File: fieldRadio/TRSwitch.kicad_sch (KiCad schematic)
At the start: 36 parts, among them Q1 MMBT3904, Q2 MMBT3904, Q3 PMV240SP, Q5 MMBT3904, Q6 PMV240SP, Q7 BSS138

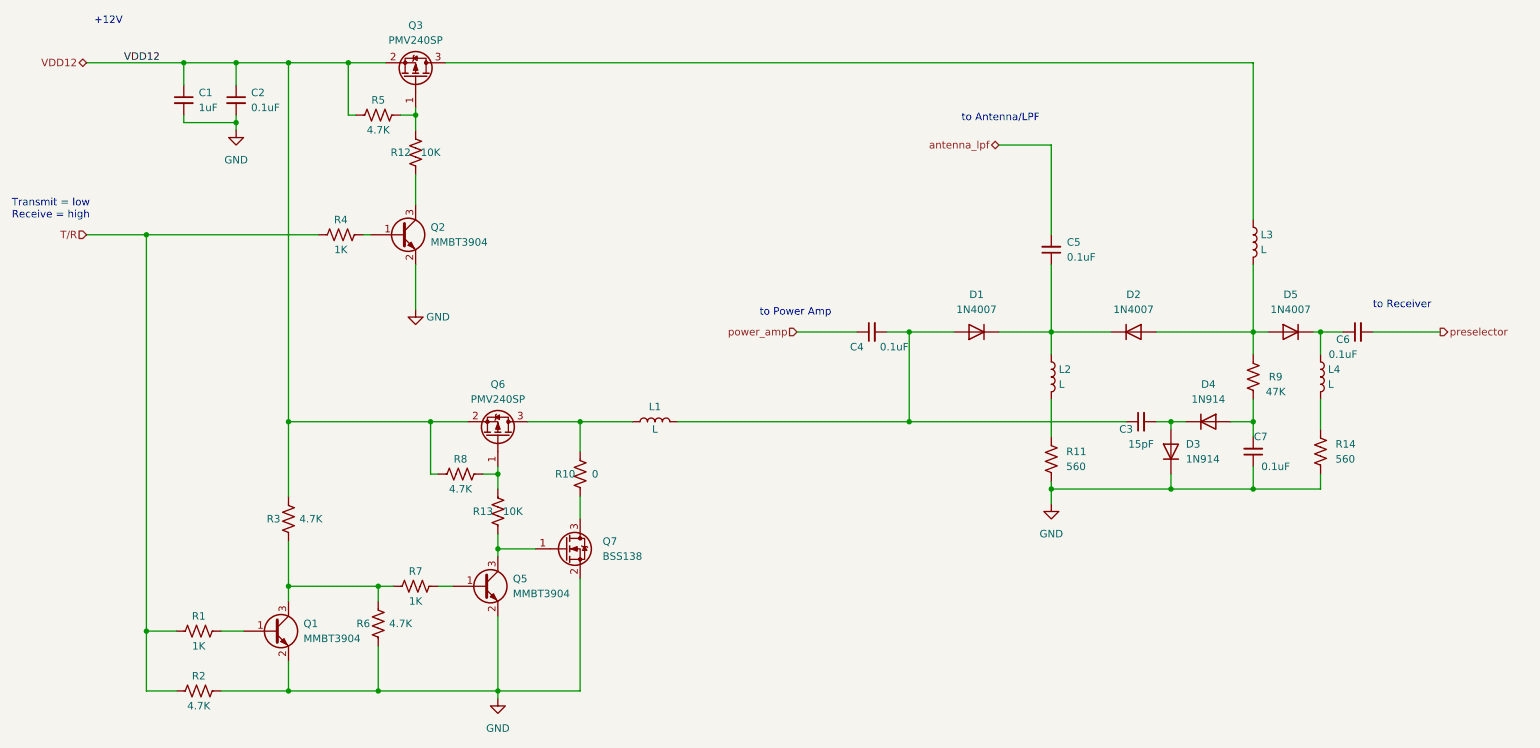
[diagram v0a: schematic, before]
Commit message: Building fieldradio schematic
in process of building field radio schematics
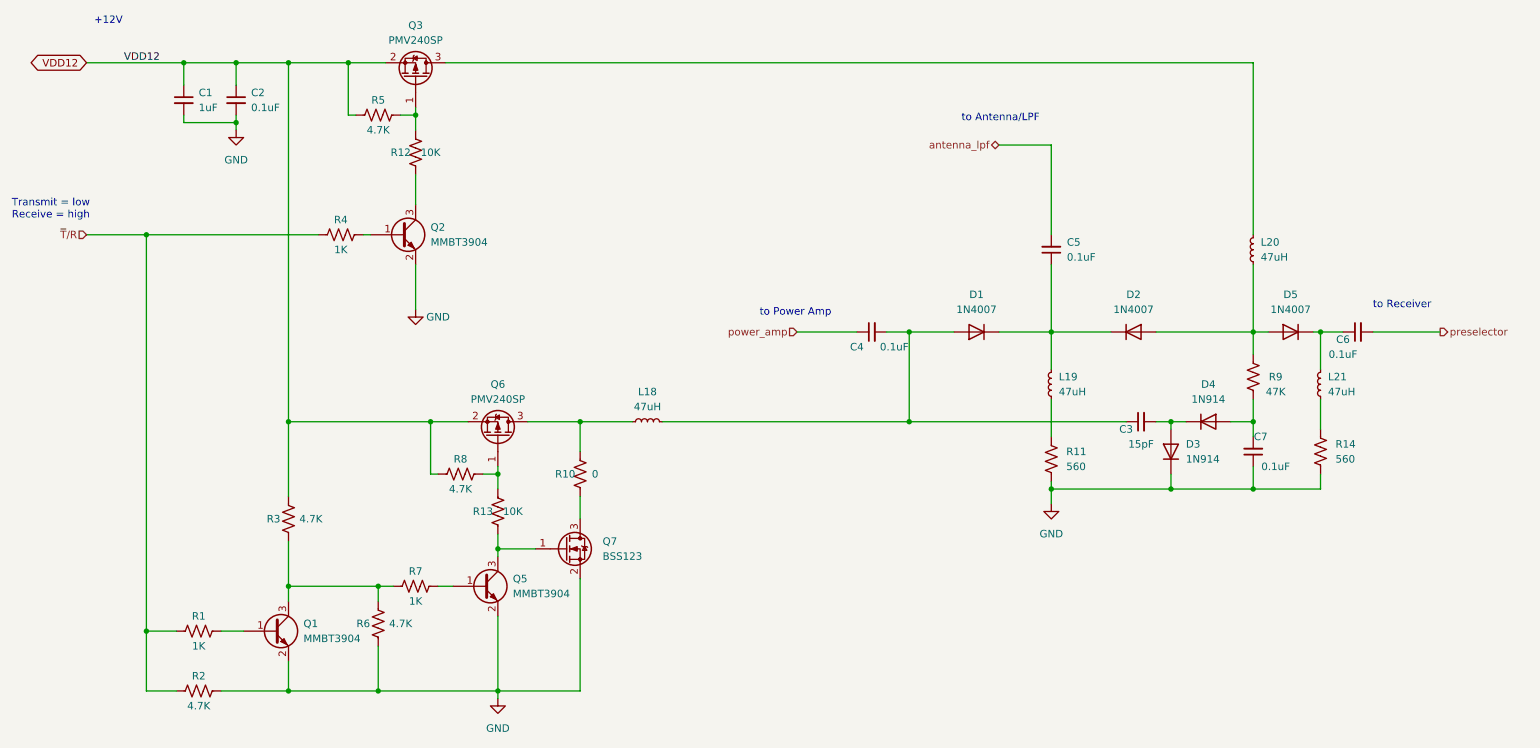
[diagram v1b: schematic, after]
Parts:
- removed L1, L2, L3, L4: L, Inductor_THT:L_Toroid_Vertical_L10.0mm_W5.0mm_P5.08mm, symbol Device:L
- added L18, L19, L20, L21: 47uH, Inductor_THT:L_Axial_L11.0mm_D4.5mm_P7.62mm_Vertical_Fastron_MECC, symbol Device:L_Small
- Q7: value BSS138 -> BSS123
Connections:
- net at C5.1, D1.1 (K), D2.1 (K): now also L19.2
- net at D2.2 (A), D5.2 (A), R9.2: now also L20.1
- net at R11.1: now also L19.1
- net at C3.1, C4.2, D1.2 (A): now also L18.2
- net at Q3.3 (D): now also L20.2
- net at Q6.3 (D), R10.2: now also L18.1
- net at R14.1: now also L21.1
- net at C6.1, D5.1 (K): now also L21.2
- net T/R renamed ~{T}/R

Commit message: More schematic dev.
More schematic development
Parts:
- renumbered L18 to L1, L19 to L2, L20 to L3, L21 to L4
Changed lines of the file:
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@@
       (project "fieldRadio"
         (path "/a1d1b2b0-2f27-4dc0-94ba-bb0e02933617/07223125-3b0c-43ef-b5d7-ce26f2ddaddd"
-          (reference "Q5") (unit 1)
+          (reference "Q4") (unit 1)
         )
       )
@@
       (project "fieldRadio"
         (path "/a1d1b2b0-2f27-4dc0-94ba-bb0e02933617/07223125-3b0c-43ef-b5d7-ce26f2ddaddd"
-          (reference "Q7") (unit 1)
+          (reference "Q6") (unit 1)
         )
       )
@@
       (project "fieldRadio"
         (path "/a1d1b2b0-2f27-4dc0-94ba-bb0e02933617/07223125-3b0c-43ef-b5d7-ce26f2ddaddd"
-          (reference "R11") (unit 1)
+          (reference "R12") (unit 1)
         )
       )
@@
       (project "fieldRadio"
         (path "/a1d1b2b0-2f27-4dc0-94ba-bb0e02933617/07223125-3b0c-43ef-b5d7-ce26f2ddaddd"
+          (reference "C3") (unit 1)
+        )
+      )
+    )
+  )
+  (symbol (lib_id "Device:C_Small") (at 265.43 100.33 180) (unit 1)
+    (in_bom yes) (on_board yes) (dnp no)
+    (property "Reference" "C5" (at 269.24 99.06 0)
+      (effects (font (size 1.27 1.27)))
+    )
+    (property "Value" "0.1uF" (at 270.51 101.6 0)
+      (effects (font (size 1.27 1.27)))
+    )
+    (property "Footprint" "Capacitor_THT:C_Disc_D5.0mm_W2.5mm_P5.00mm" (at 265.43 100.33 0)
+      (effects (font (size 1.27 1.27)) hide)
+    )
+    (property "Datasheet" "~" (at 265.43 100.33 0)
+      (effects (font (size 1.27 1.27)) hide)
+    )
+    (pin "1")
+    (pin "2")
+    (instances
+      (project ""
+        (path "/6f2c3d19-d4e9-42f1-a4a4-8f8c301ff52b"
+          (reference "C5") (unit 1)
+        )
+      )
+      (project "fieldRadio"
+        (path "/a1d1b2b0-2f27-4dc0-94ba-bb0e02933617/07223125-3b0c-43ef-b5d7-ce26f2ddaddd"
           (reference "C4") (unit 1)
         )
@@
     )
   )
-  (symbol (lib_id "Device:C_Small") (at 265.43 100.33 180) (unit 1)
-    (in_bom yes) (on_board yes) (dnp no)
-    (property "Reference" "C5" (at 269.24 99.06 0)
-      (effects (font (size 1.27 1.27)))
-    )
-    (property "Value" "0.1uF" (at 270.51 101.6 0)
-      (effects (font (size 1.27 1.27)))
-    )
-    (property "Footprint" "Capacitor_THT:C_Disc_D5.0mm_W2.5mm_P5.00mm" (at 265.43 100.33 0)
-      (effects (font (size 1.27 1.27)) hide)
-    )
-    (property "Datasheet" "~" (at 265.43 100.33 0)
-      (effects (font (size 1.27 1.27)) hide)
-    )
-    (pin "1")
-    (pin "2")
-    (instances
-      (project ""
-        (path "/6f2c3d19-d4e9-42f1-a4a4-8f8c301ff52b"
-          (reference "C5") (unit 1)
-        )
-      )
-      (project "fieldRadio"
-        (path "/a1d1b2b0-2f27-4dc0-94ba-bb0e02933617/07223125-3b0c-43ef-b5d7-ce26f2ddaddd"
-          (reference "C5") (unit 1)
-        )
-      )
-    )
-  )
   (symbol (lib_id "Device:D") (at 252.73 114.3 180) (unit 1)
     (in_bom yes) (on_board yes) (dnp no) (fields_autoplaced)
@@
   (symbol (lib_id "Device:L_Small") (at 311.15 123.19 180) (unit 1)
     (in_bom yes) (on_board yes) (dnp no) (fields_autoplaced)
-    (property "Reference" "L21" (at 312.42 121.92 0)
+    (property "Reference" "L4" (at 312.42 121.92 0)
       (effects (font (size 1.27 1.27)) (justify right))
     )
@@
       (project "fieldRadio"
         (path "/a1d1b2b0-2f27-4dc0-94ba-bb0e02933617/07223125-3b0c-43ef-b5d7-ce26f2ddaddd"
-          (reference "L21") (unit 1)
+          (reference "L4") (unit 1)
         )
       )
@@
       (project "fieldRadio"
         (path "/a1d1b2b0-2f27-4dc0-94ba-bb0e02933617/07223125-3b0c-43ef-b5d7-ce26f2ddaddd"
-          (reference "C7") (unit 1)
+          (reference "C6") (unit 1)
         )
       )
@@
       (project "fieldRadio"
         (path "/a1d1b2b0-2f27-4dc0-94ba-bb0e02933617/07223125-3b0c-43ef-b5d7-ce26f2ddaddd"
-          (reference "R12") (unit 1)
+          (reference "R7") (unit 1)
         )
       )
@@
       (project "fieldRadio"
         (path "/a1d1b2b0-2f27-4dc0-94ba-bb0e02933617/07223125-3b0c-43ef-b5d7-ce26f2ddaddd"
-          (reference "R7") (unit 1)
+          (reference "R8") (unit 1)
         )
       )
@@
       (project "fieldRadio"
         (path "/a1d1b2b0-2f27-4dc0-94ba-bb0e02933617/07223125-3b0c-43ef-b5d7-ce26f2ddaddd"
-          (reference "R10") (unit 1)
+          (reference "R11") (unit 1)
         )
       )
@@
   (symbol (lib_id "Device:L_Small") (at 299.72 100.33 180) (unit 1)
     (in_bom yes) (on_board yes) (dnp no) (fields_autoplaced)
-    (property "Reference" "L20" (at 300.99 99.06 0)
+    (property "Reference" "L3" (at 300.99 99.06 0)
       (effects (font (size 1.27 1.27)) (justify right))
     )
@@
       (project "fieldRadio"
         (path "/a1d1b2b0-2f27-4dc0-94ba-bb0e02933617/07223125-3b0c-43ef-b5d7-ce26f2ddaddd"
-          (reference "L20") (unit 1)
+          (reference "L3") (unit 1)
         )
       )
@@
       (project "fieldRadio"
         (path "/a1d1b2b0-2f27-4dc0-94ba-bb0e02933617/07223125-3b0c-43ef-b5d7-ce26f2ddaddd"
-          (reference "Q6") (unit 1)
+          (reference "Q5") (unit 1)
         )
       )
@@
   (symbol (lib_id "Device:L_Small") (at 265.43 123.19 180) (unit 1)
     (in_bom yes) (on_board yes) (dnp no) (fields_autoplaced)
-    (property "Reference" "L19" (at 266.7 121.92 0)
+    (property "Reference" "L2" (at 266.7 121.92 0)
       (effects (font (size 1.27 1.27)) (justify right))
     )
@@
       (project "fieldRadio"
         (path "/a1d1b2b0-2f27-4dc0-94ba-bb0e02933617/07223125-3b0c-43ef-b5d7-ce26f2ddaddd"
-          (reference "L19") (unit 1)
+          (reference "L2") (unit 1)
         )
       )
@@
       (project "fieldRadio"
         (path "/a1d1b2b0-2f27-4dc0-94ba-bb0e02933617/07223125-3b0c-43ef-b5d7-ce26f2ddaddd"
-          (reference "#PWR07") (unit 1)
+          (reference "#PWR05") (unit 1)
         )
       )
@@
       (project "fieldRadio"
         (path "/a1d1b2b0-2f27-4dc0-94ba-bb0e02933617/07223125-3b0c-43ef-b5d7-ce26f2ddaddd"
-          (reference "R8") (unit 1)
+          (reference "R9") (unit 1)
         )
       )
@@
       (project "fieldRadio"
         (path "/a1d1b2b0-2f27-4dc0-94ba-bb0e02933617/07223125-3b0c-43ef-b5d7-ce26f2ddaddd"
-          (reference "C6") (unit 1)
+          (reference "C7") (unit 1)
         )
       )
@@
   (symbol (lib_id "Device:L_Small") (at 196.85 129.54 90) (unit 1)
     (in_bom yes) (on_board yes) (dnp no) (fields_autoplaced)
-    (property "Reference" "L18" (at 196.85 124.46 90)
+    (property "Reference" "L1" (at 196.85 124.46 90)
       (effects (font (size 1.27 1.27)))
     )
@@
       (project "fieldRadio"
         (path "/a1d1b2b0-2f27-4dc0-94ba-bb0e02933617/07223125-3b0c-43ef-b5d7-ce26f2ddaddd"
-          (reference "L18") (unit 1)
+          (reference "L1") (unit 1)
         )
       )
@@
       (project "fieldRadio"
         (path "/a1d1b2b0-2f27-4dc0-94ba-bb0e02933617/07223125-3b0c-43ef-b5d7-ce26f2ddaddd"
-          (reference "C3") (unit 1)
+          (reference "C5") (unit 1)
         )
       )
@@
       (project "fieldRadio"
         (path "/a1d1b2b0-2f27-4dc0-94ba-bb0e02933617/07223125-3b0c-43ef-b5d7-ce26f2ddaddd"
+          (reference "R10") (unit 1)
+        )
+      )
+    )
+  )
+  (symbol (lib_id "Device:R_US") (at 299.72 121.92 180) (unit 1)
+    (in_bom yes) (on_board yes) (dnp no)
+    (property "Reference" "R9" (at 303.53 121.92 0)
+      (effects (font (size 1.27 1.27)))
+    )
+    (property "Value" "47K" (at 303.53 124.46 0)
+      (effects (font (size 1.27 1.27)))
+    )
+    (property "Footprint" "Resistor_SMD:R_0603_1608Metric_Pad0.98x0.95mm_HandSolder" (at 298.704 121.666 90)
+      (effects (font (size 1.27 1.27)) hide)
+    )
+    (property "Datasheet" "~" (at 299.72 121.92 0)
+      (effects (font (size 1.27 1.27)) hide)
+    )
+    (pin "1")
+    (pin "2")
+    (instances
+      (project ""
+        (path "/6f2c3d19-d4e9-42f1-a4a4-8f8c301ff52b"
+          (reference "R9") (unit 1)
+        )
+      )
+      (project "fieldRadio"
+        (path "/a1d1b2b0-2f27-4dc0-94ba-bb0e02933617/07223125-3b0c-43ef-b5d7-ce26f2ddaddd"
           (reference "R13") (unit 1)
         )
       )
-    )
-  )
-  (symbol (lib_id "Device:R_US") (at 299.72 121.92 180) (unit 1)
-    (in_bom yes) (on_board yes) (dnp no)
-    (property "Reference" "R9" (at 303.53 121.92 0)
-      (effects (font (size 1.27 1.27)))
-    )
-    (property "Value" "47K" (at 303.53 124.46 0)
-      (effects (font (size 1.27 1.27)))
-    )
-    (property "Footprint" "Resistor_SMD:R_0603_1608Metric_Pad0.98x0.95mm_HandSolder" (at 298.704 121.666 90)
-      (effects (font (size 1.27 1.27)) hide)
-    )
-    (property "Datasheet" "~" (at 299.72 121.92 0)
-      (effects (font (size 1.27 1.27)) hide)
-    )
-    (pin "1")
-    (pin "2")
-    (instances
-      (project ""
-        (path "/6f2c3d19-d4e9-42f1-a4a4-8f8c301ff52b"
-          (reference "R9") (unit 1)
-        )
-      )
-      (project "fieldRadio"
-        (path "/a1d1b2b0-2f27-4dc0-94ba-bb0e02933617/07223125-3b0c-43ef-b5d7-ce26f2ddaddd"
-          (reference "R9") (unit 1)
-        )
-      )
